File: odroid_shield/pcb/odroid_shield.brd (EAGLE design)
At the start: 83 x 48 mm, 71 parts, among them J1 AVRISP6_COMPACT, J4 ODROID_J4, U1 SINGLE-BIT_BUS_TRANSCEIVER, U10 ABM8G, U2 SINGLE-BIT_BUS_TRANSCEIVER, U3 ST1S10, U4 ATMEGA644P-20AU, U5 TS5205, U6 TCA9517MSOP8, U7 MP33926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

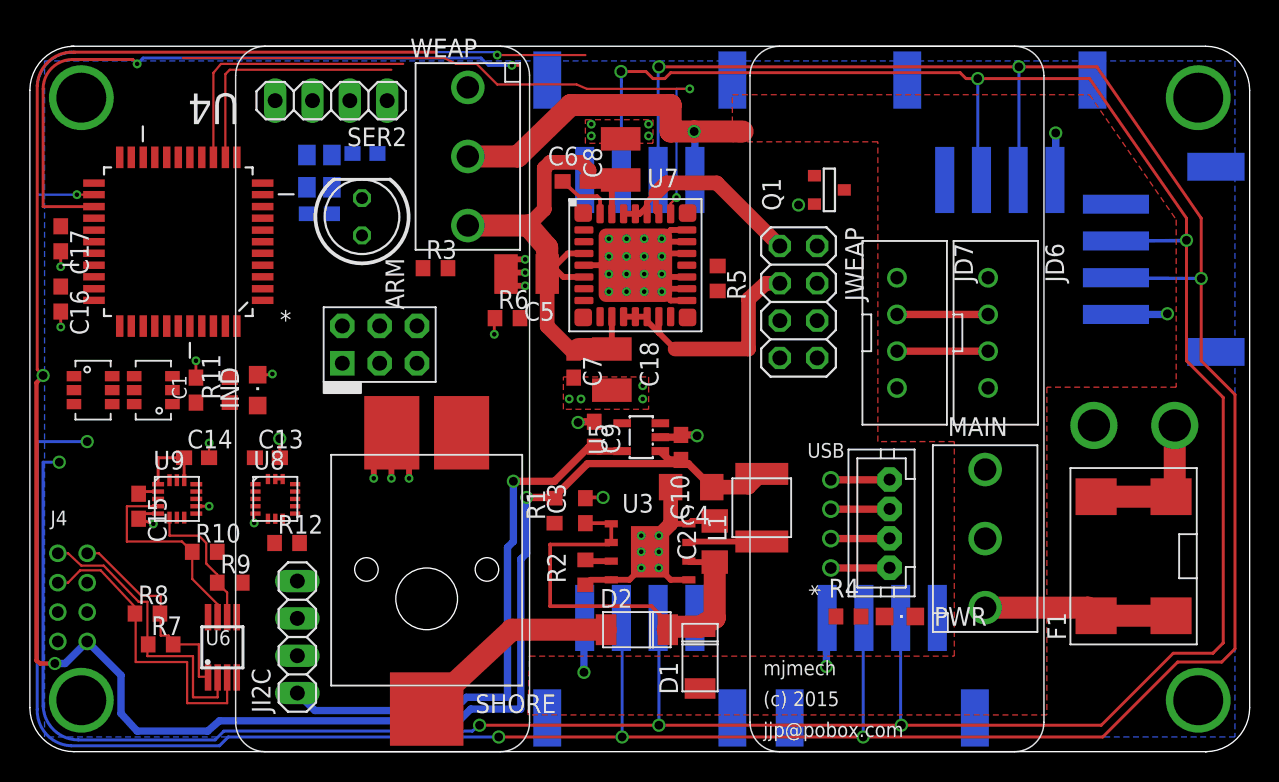
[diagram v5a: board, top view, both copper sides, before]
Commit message: odroid_shield: First pass at silk sizing and placement, pre autoroute.
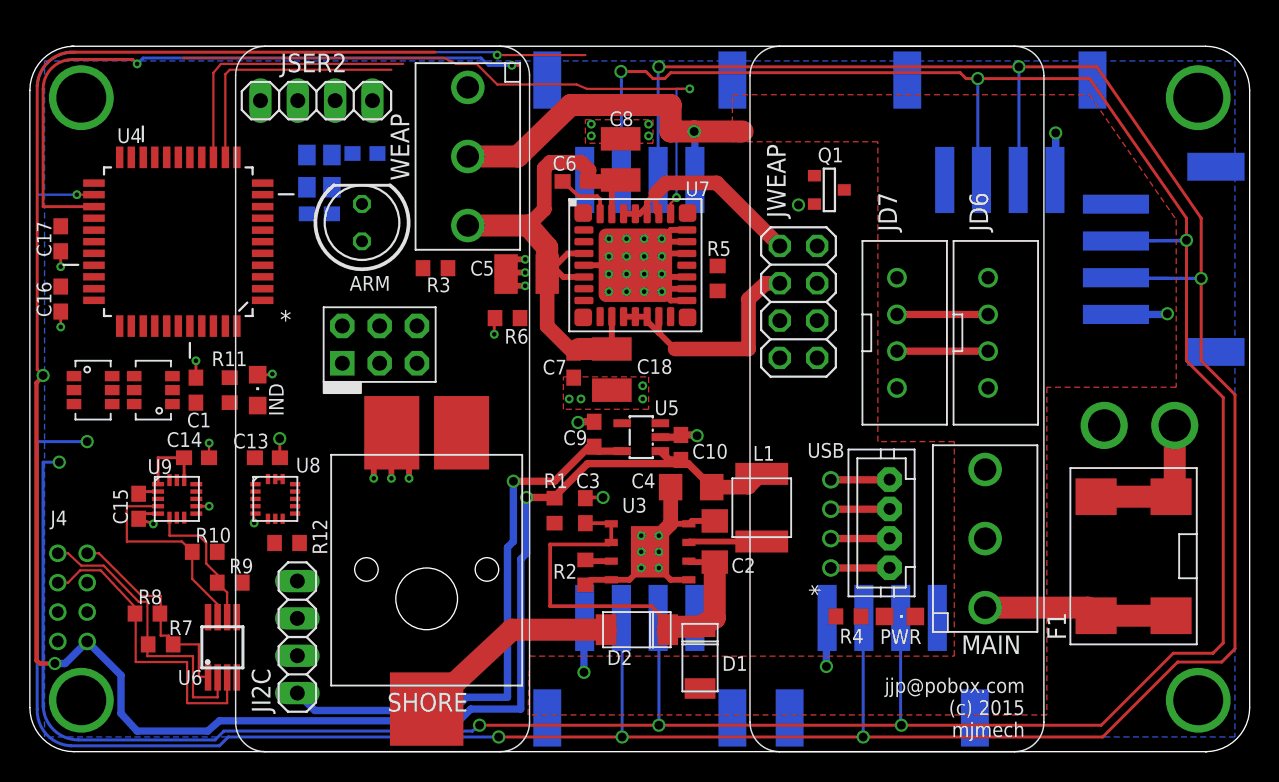
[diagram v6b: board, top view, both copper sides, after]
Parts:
- removed SER2: (no value), pinhead:1X04
- added JSER2: (no value), pinhead:1X04
- moved B- 0.70 mm to (73.1, 22.2)
- moved ARM 0.40 mm to (22.6, 36.0)
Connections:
- net +5V: now also JSER2.4; no longer SER2.4
- net GND: now also JSER2.1; no longer SER2.1
- net N$26: now also JSER2.3; no longer SER2.3
- net N$27: now also JSER2.2; no longer SER2.2

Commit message: odroid_shield: More silk tweaks.
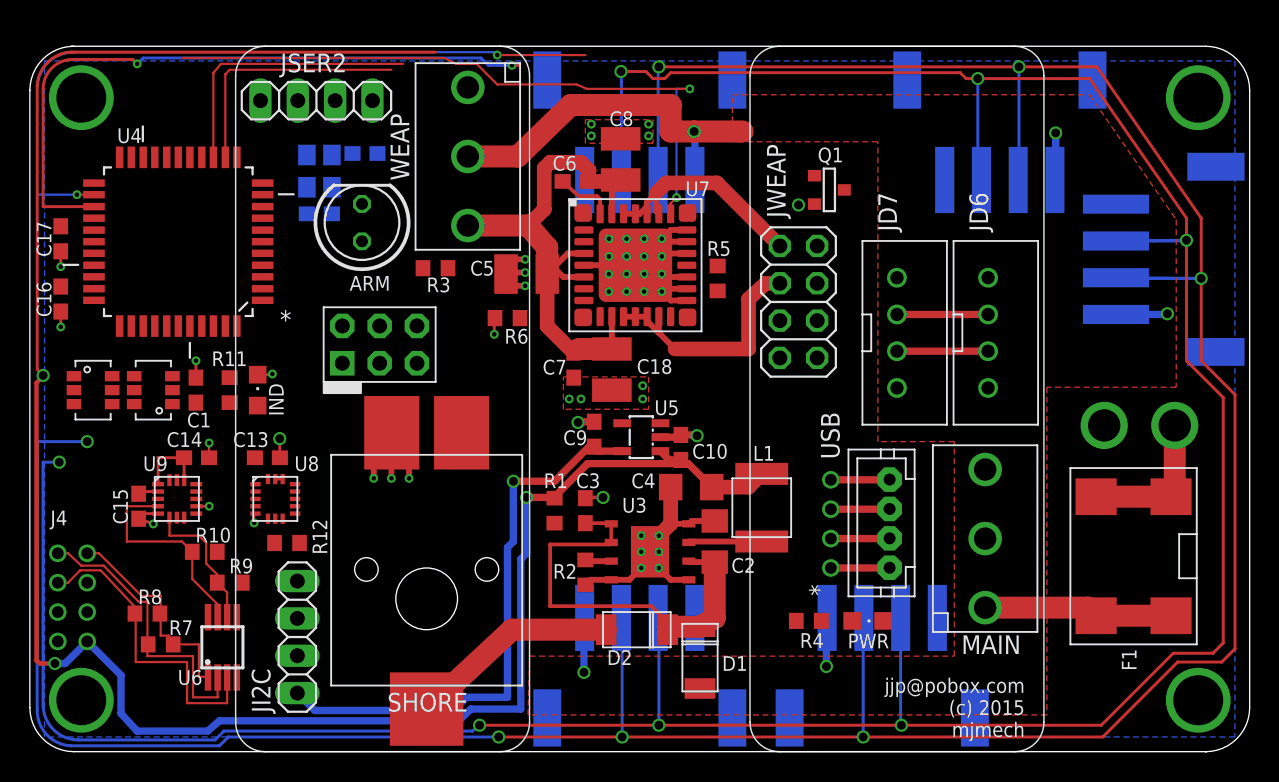
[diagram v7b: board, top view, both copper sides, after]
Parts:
- moved R4 2.72 mm to (53.0, 8.90)
- moved PWR 2.22 mm to (57.0, 8.90)
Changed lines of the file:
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@@
 <wire x1="83" y1="3" x2="83" y2="45" width="0" layer="20"/>
 <text x="1.4" y="15.4" size="1" layer="21" ratio="10">J4</text>
-<text x="52.9" y="20" size="1" layer="21" ratio="10">USB</text>
+<text x="55.1" y="19.9" size="1.27" layer="21" rot="R90">USB</text>
 <wire x1="49" y1="46" x2="49" y2="2" width="0.1" layer="21"/>
 <wire x1="49" y1="2" x2="51" y2="0" width="0.1" layer="21" curve="90"/>
@@
 </element>
 <element name="JWEAP" library="pinhead" package="2X04" value="" x="52.3" y="30.6" smashed="yes" rot="R270">
-<attribute name="NAME" x="51.425" y="36.32" size="1.27" layer="25" ratio="10" rot="R90"/>
+<attribute name="NAME" x="51.425" y="36.32" size="1.27" layer="25" rot="R90"/>
 <attribute name="VALUE" x="47.855" y="35.68" size="1.27" layer="27" rot="R270"/>
 </element>
@@
 <attribute name="NAME" x="24.525" y="32.3666" size="1" layer="25" ratio="10" rot="R180"/>
 </element>
-<element name="PWR" library="led" package="CHIPLED_0805" value="GREEN" x="59.2" y="9.2" smashed="yes" rot="R270">
-<attribute name="NAME" x="60.67" y="8.33" size="1" layer="25" ratio="10" rot="R180"/>
+<element name="PWR" library="led" package="CHIPLED_0805" value="GREEN" x="57" y="8.9" smashed="yes" rot="R270">
+<attribute name="NAME" x="58.47" y="8.03" size="1" layer="25" ratio="10" rot="R180"/>
 </element>
 <element name="SHORE" library="odroid_shield" package="CUI_PJ_015AH_SMT" value="PJ-034ASMT" x="27" y="10.4" smashed="yes" rot="R180">
@@
 </element>
 <element name="JI2C" library="pinhead" package="1X04" value="" x="18.2" y="7.8" rot="R90"/>
-<element name="F1" library="odroid_shield" package="KEYSTONE_HORIZ_FUSE_CLIP" value="FUSE" x="75.1" y="13.3" rot="R90">
+<element name="F1" library="odroid_shield" package="KEYSTONE_HORIZ_FUSE_CLIP" value="FUSE" x="75.1" y="13.3" smashed="yes" rot="R90">
 <attribute name="DPN" value="36-3569-ND" x="75.1" y="13.3" size="1.778" layer="27" rot="R90" display="off"/>
+<attribute name="NAME" x="74.3" y="7" size="1" layer="21" ratio="10" rot="R270"/>
 </element>
 <element name="U3" library="odroid_shield" package="POWER_SO8" value="ST1S10" x="42.2" y="13.6" smashed="yes" rot="R270">
@@
 <attribute name="NAME" x="28.635" y="32.265" size="1" layer="25" ratio="10" rot="R180"/>
 </element>
-<element name="R4" library="rcl" package="R0603" value="500" x="55.7" y="9.2" smashed="yes" rot="R180">
-<attribute name="NAME" x="56.735" y="8.365" size="1" layer="25" ratio="10" rot="R180"/>
+<element name="R4" library="rcl" package="R0603" value="500" x="53" y="8.9" smashed="yes" rot="R180">
+<attribute name="NAME" x="54.035" y="8.065" size="1" layer="25" ratio="10" rot="R180"/>
 </element>
 <element name="U7" library="odroid_shield" package="PQFN32" value="MP33926" x="41.2" y="33.1" smashed="yes">
@@
 <element name="JSER2" library="pinhead" package="1X04" value="" x="19.5" y="44.3" smashed="yes" rot="R180">
 <attribute name="DPN" value="S9410-ND" x="19.5" y="44.3" size="1" layer="27" ratio="10" rot="R180" display="off"/>
-<attribute name="NAME" x="17.0438" y="46.2288" size="1.27" layer="25" ratio="10"/>
+<attribute name="NAME" x="17.0438" y="46.2288" size="1.27" layer="25"/>
 <attribute name="VALUE" x="24.58" y="47.475" size="1.27" layer="27" rot="R180"/>
 </element>
@@
 </element>
 <element name="U8" library="odroid_shield" package="LGA16" value="MAX21000" x="16.7" y="17.2" smashed="yes">
-<attribute name="NAME" x="18.1" y="19" size="1" layer="21" ratio="10"/>
+<attribute name="NAME" x="18" y="19.1" size="1" layer="21" ratio="10"/>
 </element>
 <element name="R12" library="rcl" package="R0603" value="100k" x="17.5" y="14.2" smashed="yes">
@@
 </element>
 <element name="C13" library="rcl" package="C0603" value=".1uF" x="16.16" y="20" smashed="yes">
-<attribute name="NAME" x="13.825" y="20.635" size="1" layer="25" ratio="10"/>
+<attribute name="NAME" x="13.825" y="20.735" size="1" layer="25" ratio="10"/>
 </element>
 <element name="U9" library="odroid_shield" package="QFN16" value="MMA8451Q" x="10" y="17.2" smashed="yes">
-<attribute name="NAME" x="8" y="18.9" size="1" layer="21" ratio="10"/>
+<attribute name="NAME" x="7.7" y="19.1" size="1" layer="21" ratio="10"/>
 </element>
 <element name="C14" library="rcl" package="C0603" value=".1uF" x="11.34" y="20" smashed="yes">
@@
 <wire x1="41.2" y1="33.1" x2="40.6" y2="32.5" width="0" layer="19" extent="1-1"/>
 <wire x1="11.325" y1="17.7" x2="11.325" y2="16.7" width="0" layer="19" extent="1-1"/>
-<wire x1="60.25" y1="9.2" x2="61.75" y2="9.1" width="0" layer="19" extent="1-16"/>
 <wire x1="9.7" y1="24.6" x2="11.3" y2="25.45" width="0" layer="19" extent="1-1"/>
 <wire x1="4.3596" y1="34.7" x2="2.1" y2="34.05" width="0" layer="19" extent="1-1"/>
 <wire x1="10.1" y1="28.9596" x2="11.3" y2="26.6" width="0" layer="19" extent="1-1"/>
+<wire x1="58.05" y1="8.9" x2="61.75" y2="9.1" width="0" layer="19" extent="1-16"/>
 <wire x1="3" y1="24.6" x2="2.1" y2="28.9" width="0" layer="19" extent="1-1"/>
 <wire x1="15.8404" y1="34.7" x2="20.55" y2="36.6" width="0" layer="19" extent="1-16"/>
@@
 <wire x1="43.6" y1="42.2" x2="43.6" y2="44" width="1.5" layer="1"/>
 <wire x1="45.2" y1="42.2" x2="48.5" y2="42.2" width="1.5" layer="1"/>
-<wire x1="54.25" y1="9.1" x2="54.85" y2="9.2" width="0" layer="19" extent="1-16"/>
+<wire x1="54.2" y1="9.1" x2="52.15" y2="8.9" width="0" layer="19" extent="1-16"/>
 </signal>
 <signal name="N$9">
@@
 <contactref element="R4" pad="1"/>
 <contactref element="PWR" pad="A"/>
-<wire x1="58.15" y1="9.2" x2="56.55" y2="9.2" width="0" layer="19" extent="1-1"/>
+<wire x1="53.85" y1="8.9" x2="55.95" y2="8.9" width="0" layer="19" extent="1-1"/>
 </signal>
 <signal name="N$16">
